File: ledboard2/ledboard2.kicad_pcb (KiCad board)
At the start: 2 copper layers, 161 x 170 mm, 109 parts, among them P1 CONN_01X03, P2 CONN_01X03, U1 NEOPIXEL, U10 NEOPIXEL, U100 NEOPIXEL, U11 NEOPIXEL, U12 NEOPIXEL, U13 NEOPIXEL, U14 NEOPIXEL, U15 NEOPIXEL, U16 NEOPIXEL, U17 NEOPIXEL, U18 NEOPIXEL, U19 NEOPIXEL, U2 NEOPIXEL, U20 NEOPIXEL, U21 NEOPIXEL, U22 NEOPIXEL, U23 NEOPIXEL, U24 NEOPIXEL, U25 NEOPIXEL, U26 NEOPIXEL, U27 NEOPIXEL, U28 NEOPIXEL, U29 NEOPIXEL, U3 NEOPIXEL, U30 NEOPIXEL, U31 NEOPIXEL, U32 NEOPIXEL, U33 NEOPIXEL, U34 NEOPIXEL, U35 NEOPIXEL, U36 NEOPIXEL, U37 NEOPIXEL, U38 NEOPIXEL, U39 NEOPIXEL, U4 NEOPIXEL, U40 NEOPIXEL, U41 NEOPIXEL, U42 NEOPIXEL, U43 NEOPIXEL, U44 NEOPIXEL, U45 NEOPIXEL, U46 NEOPIXEL, U47 NEOPIXEL, U48 NEOPIXEL, U49 NEOPIXEL, U5 NEOPIXEL, U50 NEOPIXEL, U51 NEOPIXEL, U52 NEOPIXEL, U53 NEOPIXEL, U54 NEOPIXEL, U55 NEOPIXEL, U56 NEOPIXEL, U57 NEOPIXEL, U58 NEOPIXEL, U59 NEOPIXEL, U6 NEOPIXEL, U60 NEOPIXEL, U61 NEOPIXEL, U62 NEOPIXEL, U63 NEOPIXEL, U64 NEOPIXEL, U65 NEOPIXEL, U66 NEOPIXEL, U67 NEOPIXEL, U68 NEOPIXEL, U69 NEOPIXEL, U7 NEOPIXEL, U70 NEOPIXEL, U71 NEOPIXEL, U72 NEOPIXEL, U73 NEOPIXEL, U74 NEOPIXEL, U75 NEOPIXEL, U76 NEOPIXEL, U77 NEOPIXEL, U78 NEOPIXEL, U79 NEOPIXEL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

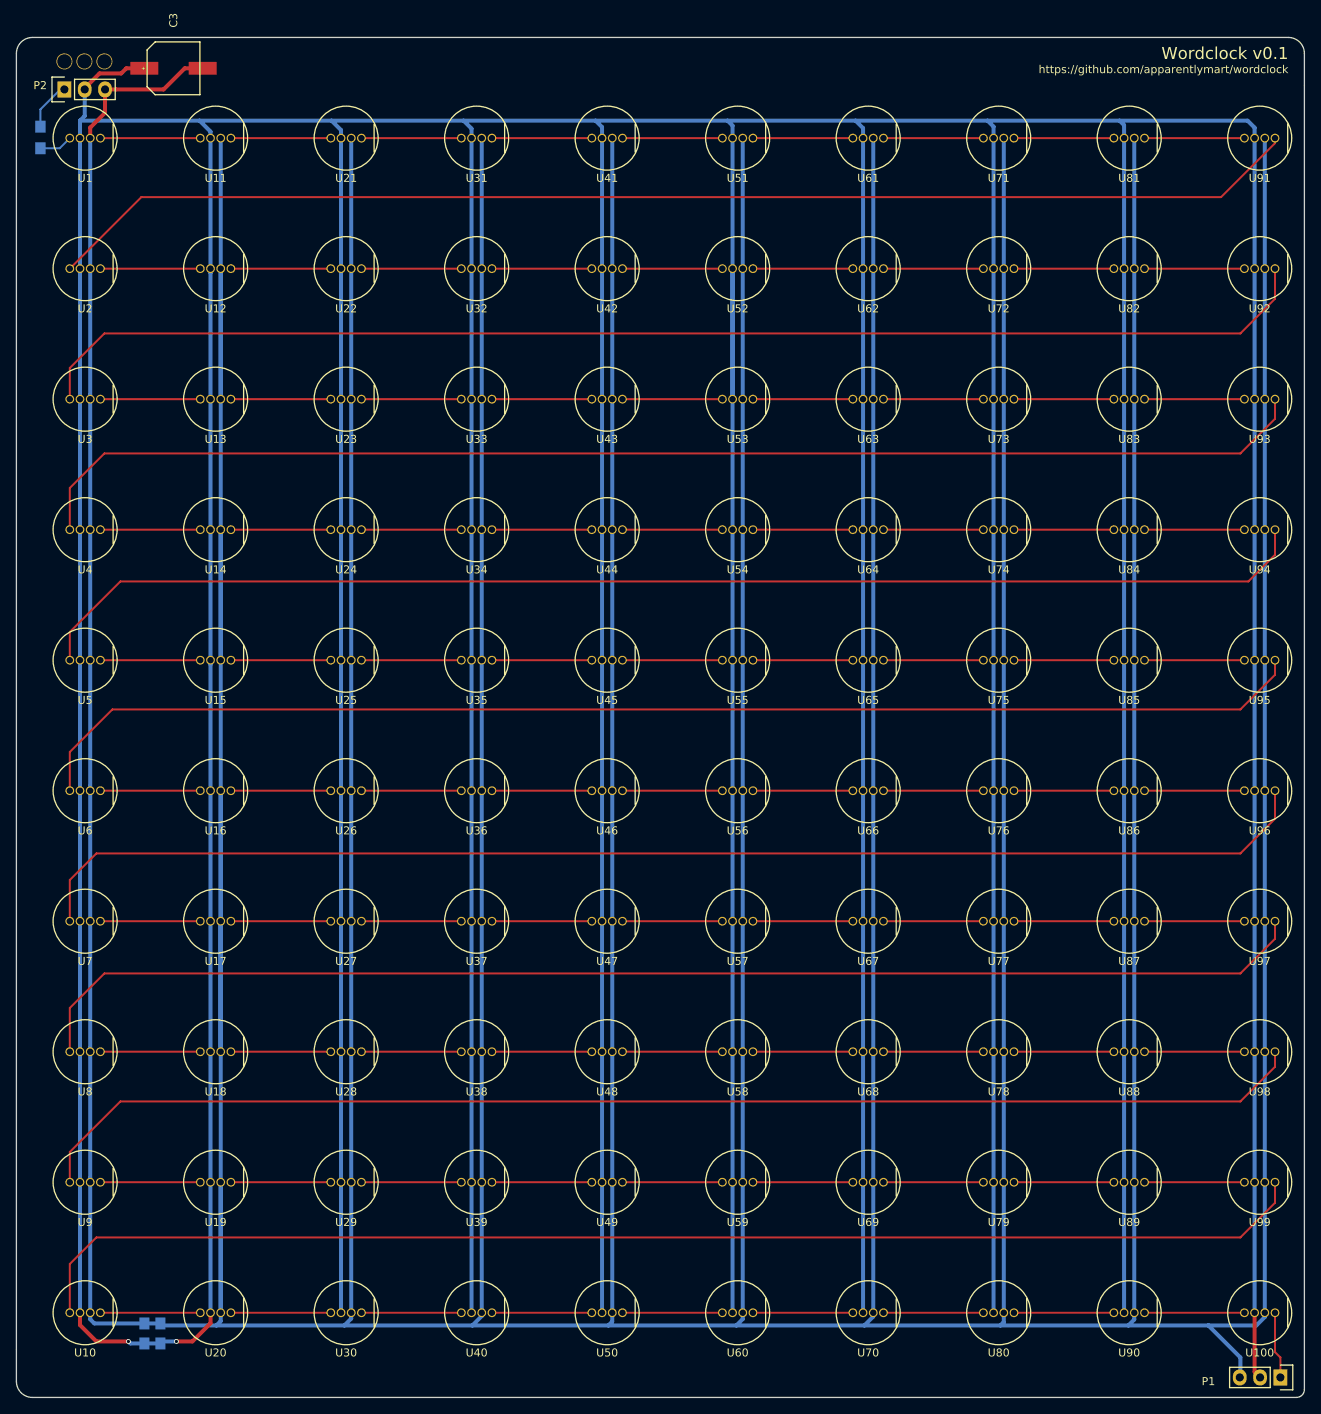
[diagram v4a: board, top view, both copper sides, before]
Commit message: Add filled zones.
These aren't really serving any electrical purpose, but since these boards
are being manufactured very thin they are quite translucent where no
copper is present.
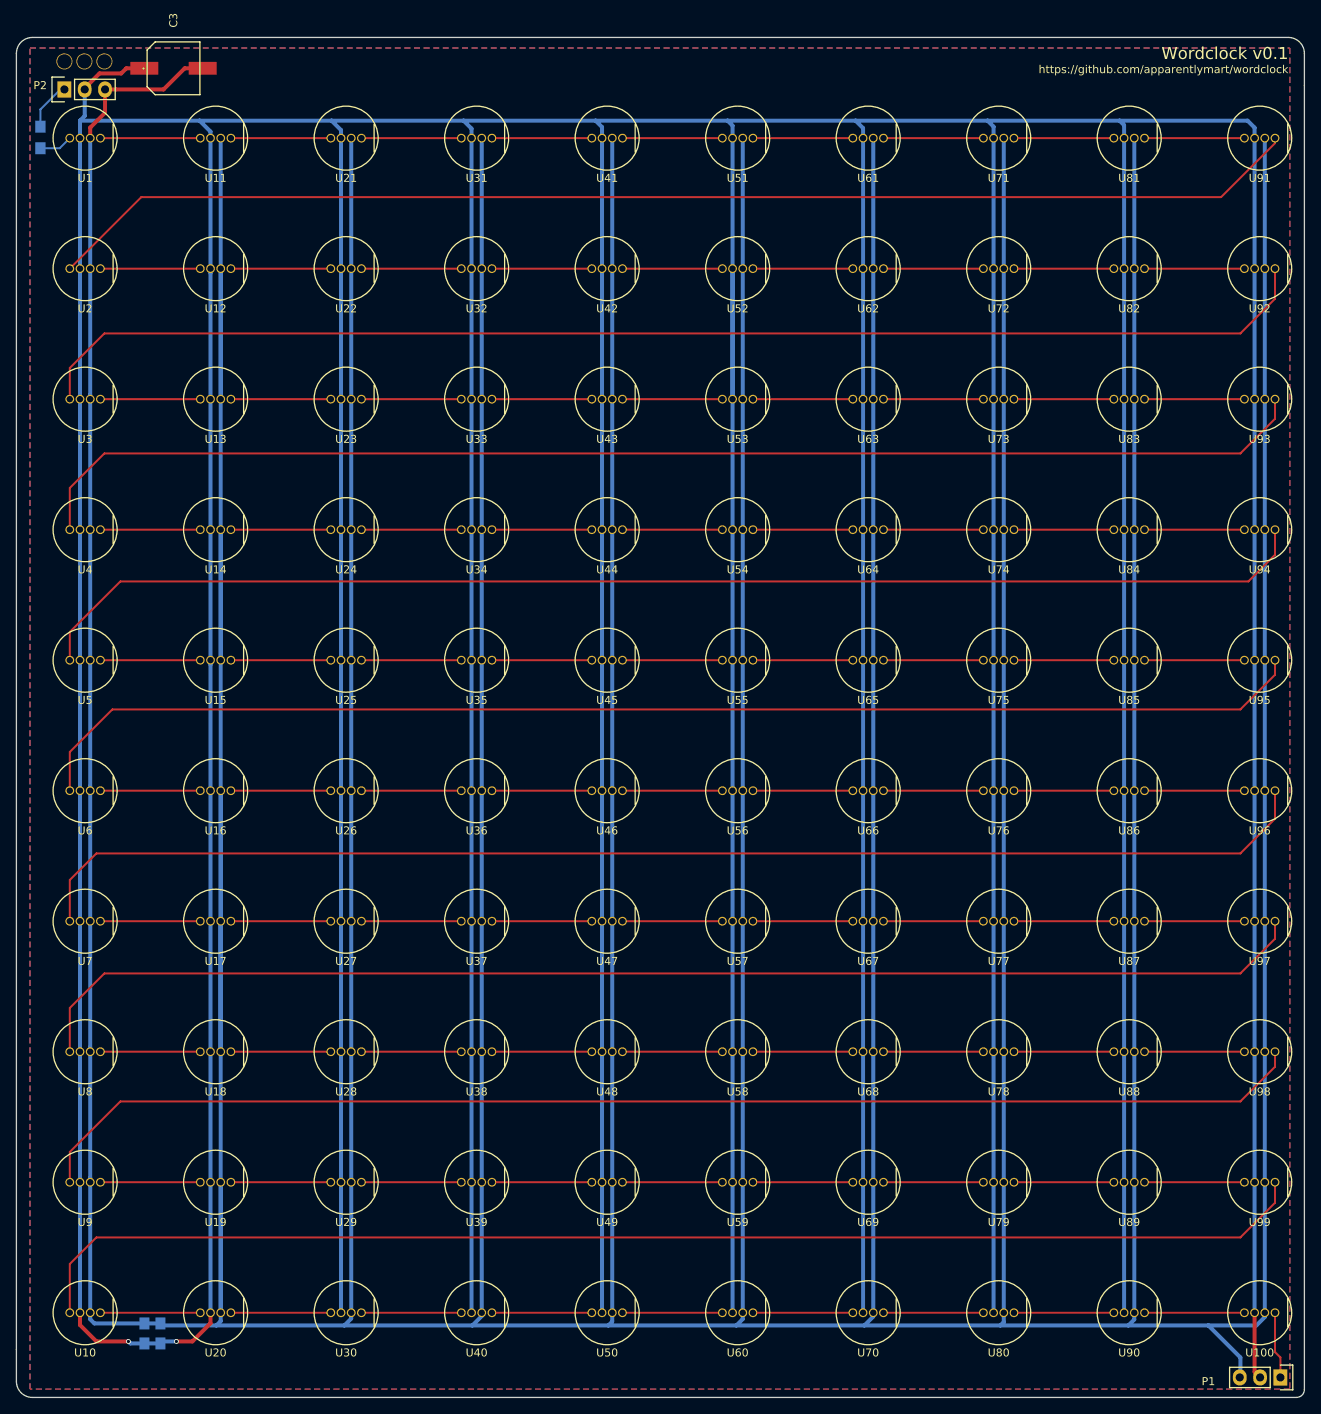
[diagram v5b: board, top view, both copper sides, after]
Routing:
- added copper zone on F.Cu, net +5V
- added copper zone on B.Cu, net GND
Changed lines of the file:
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@@
   (segment (start 152.0115 162.099) (end 164.5005 162.099) (width 0.25) (layer F.Cu) (net 103))
   (segment (start 152.0115 178.413) (end 164.5005 178.413) (width 0.25) (layer F.Cu) (net 104))
+  (zone (net 2) (net_name GND) (layer B.Cu) (hatch edge 0.508)
+    (connect_pads (clearance 0.508))
+    (min_thickness 0.254)
+    (fill yes (arc_segments 16) (thermal_gap 0.508) (thermal_bridge_width 0.508))
+    (polygon
+      (pts
+        (xy 12.7 20.32) (xy 170.18 20.32) (xy 170.18 187.96) (xy 12.7 187.96)
+      )
+    )
+  )
+  (zone (net 1) (net_name +5V) (layer F.Cu) (hatch edge 0.508)
+    (connect_pads (clearance 0.508))
+    (min_thickness 0.254)
+    (fill yes (arc_segments 16) (thermal_gap 0.508) (thermal_bridge_width 0.508))
+    (polygon
+      (pts
+        (xy 12.7 20.32) (xy 170.18 20.32) (xy 170.18 187.96) (xy 12.7 187.96)
+      )
+    )
+  )
 )

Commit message: Bump revision to v0.2.
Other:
- board text added: "Wordclock v0.2"
- board text removed: "Wordclock v0.1"
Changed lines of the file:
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@@
     (effects (font (size 1 1) (thickness 0.25)) (justify right))
   )
-  (gr_text "Wordclock v0.1" (at 170 21) (layer F.SilkS)
+  (gr_text "Wordclock v0.2" (at 170 21) (layer F.SilkS)
     (effects (font (size 1.5 1.5) (thickness 0.3)) (justify right))
   )

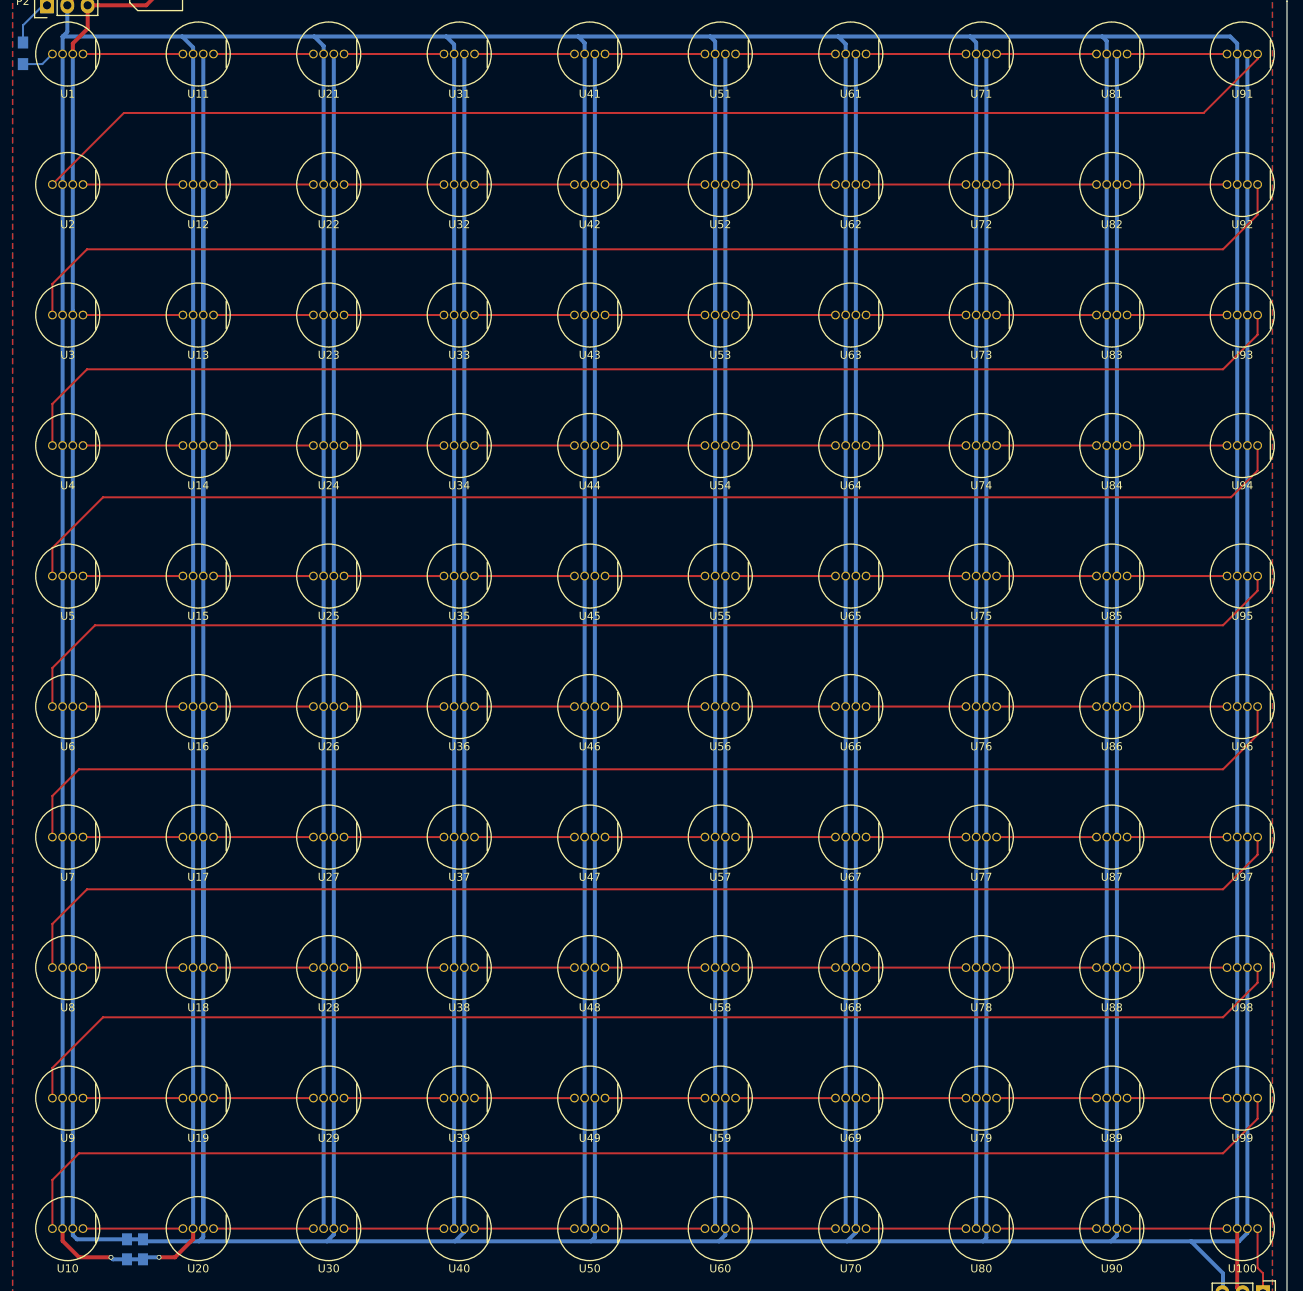
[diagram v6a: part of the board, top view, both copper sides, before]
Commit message: Tweak the pad sizes on the Neopixel footprints.
Making them a little narrower but a lot taller should make them less
likely to short while easier to solder.
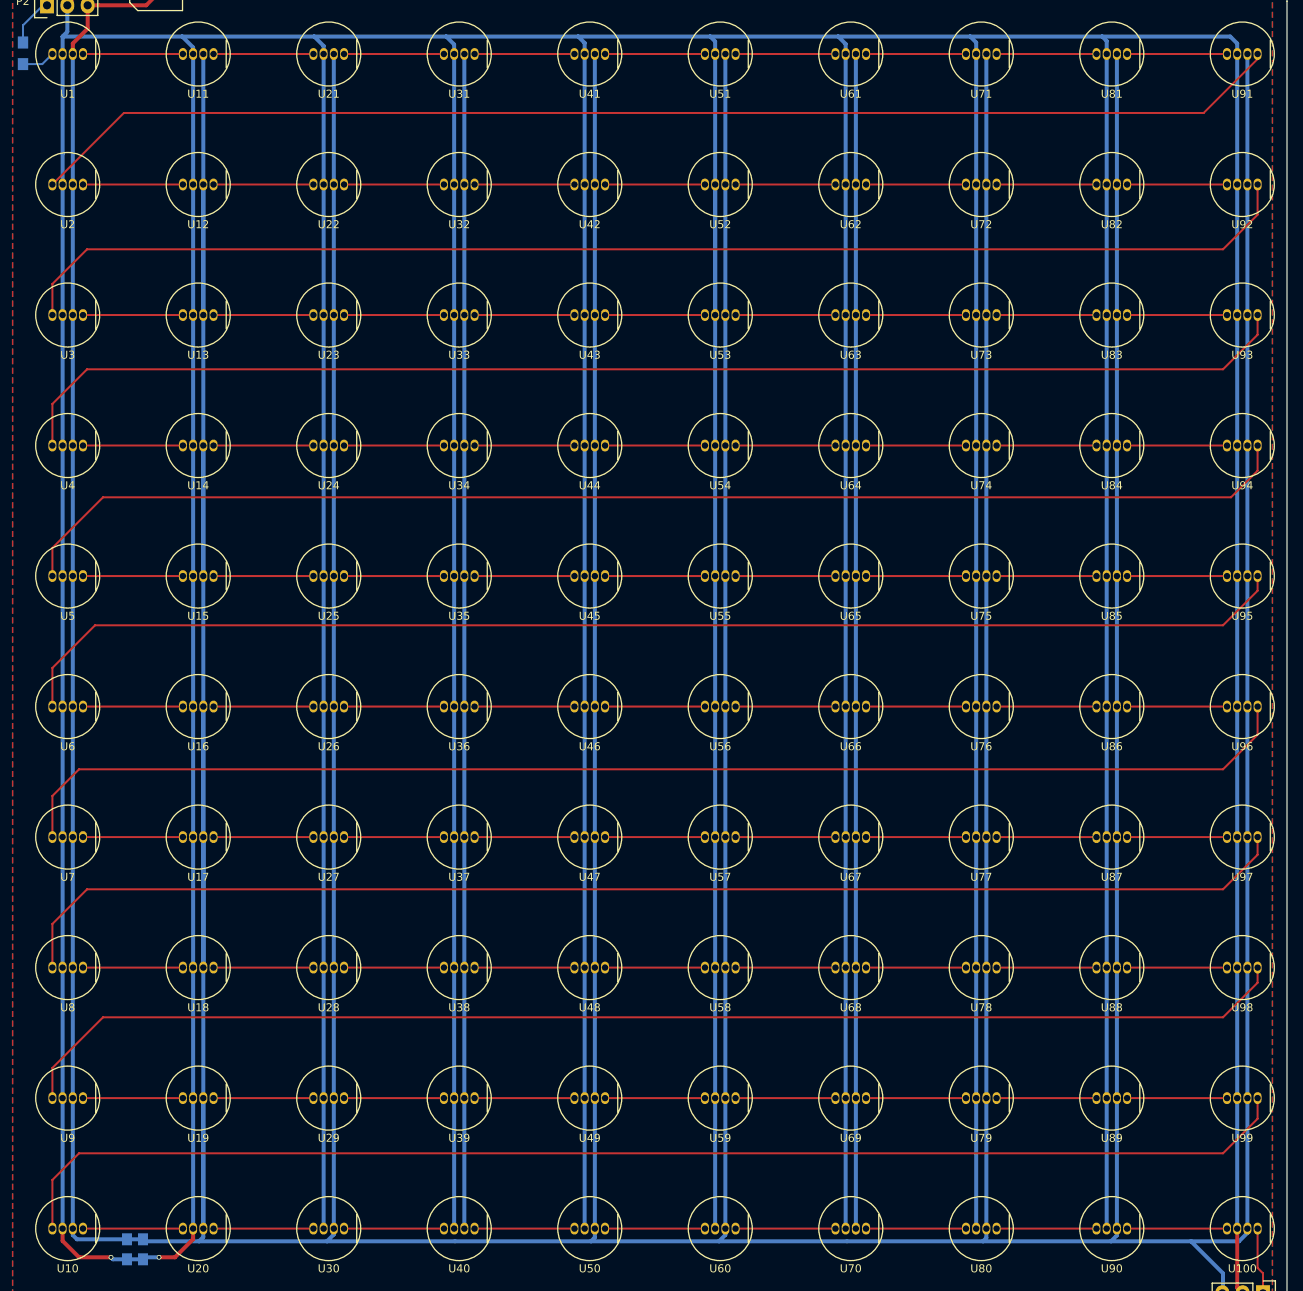
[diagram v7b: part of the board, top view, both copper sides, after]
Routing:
- net GND: track 1759.3 -> 1756.1 mm
